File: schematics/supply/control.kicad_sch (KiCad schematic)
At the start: 102 parts, among them J10 Conn_01x04_Pin, J11 Conn_01x04_Pin, J12 Conn_01x04_Pin, J13 Conn_01x04_Pin, J14 USBASP, J15 USBASP, J16 JST XH B3B, J17 Conn_01x06_Pin, J18 Conn_01x03_Pin, J19 Conn_01x06_Pin, M1 Fan, Q10 IRLML5203, Q3 IRLML0030, Q4 IRLML0030, Q6 IRLML0030, SW1 EC11W****, SW3 SW_Push, U14 ATmega328-A, U15 ATtiny1616-M, U16 Display_1.18inch_st7535, U17 AD9833xRM, U18 MCP4726A0T-E/CH, U19 MAX961, U20 LM158DR, U21 FAN3100, X1 HC-49U, 16MHz, X2 25 MHz

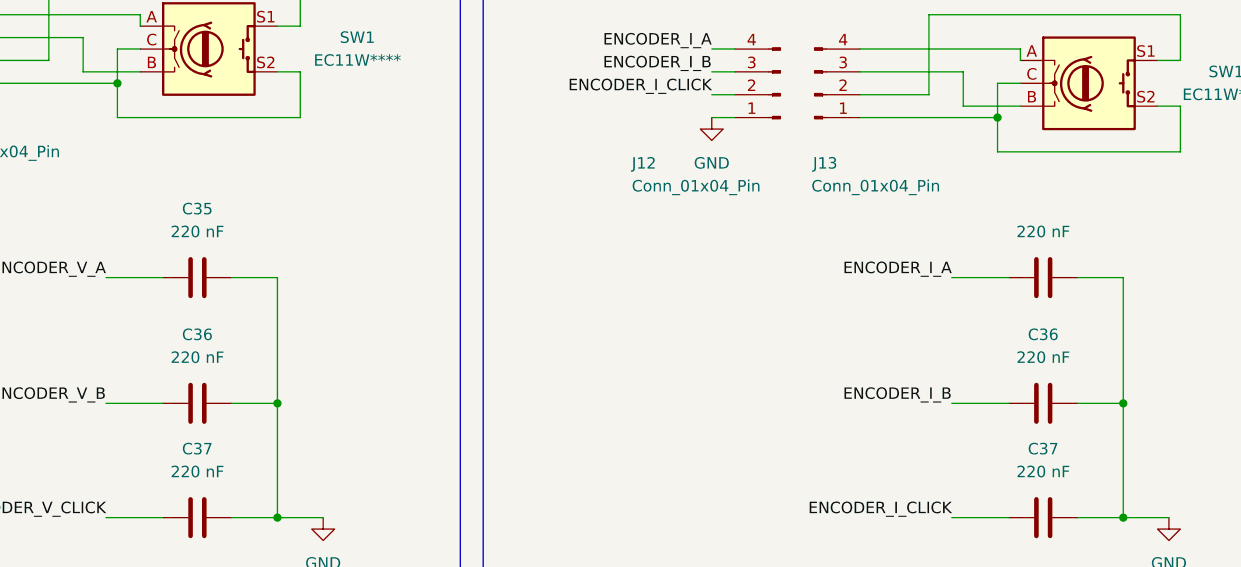
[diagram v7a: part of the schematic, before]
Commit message: some changes in schema. I found additional error. This commit saves changes before re-write some blocks
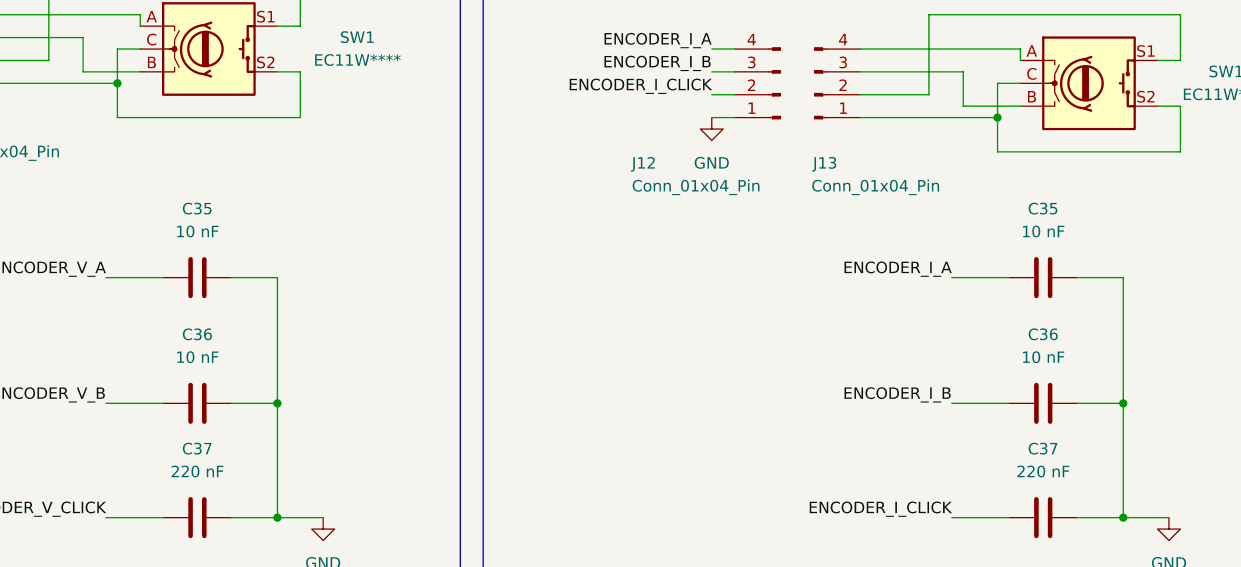
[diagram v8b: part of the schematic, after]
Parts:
- C35, C36: value 220 nF -> 10 nF
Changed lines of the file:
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@@
 			)
 		)
-		(property "Value" "220 nF"
+		(property "Value" "10 nF"
 			(at 77.47 165.1 90)
 			(effects
@@
 					(size 1.27 1.27)
 				)
-				(hide yes)
 			)
 		)
-		(property "Value" "220 nF"
+		(property "Value" "10 nF"
 			(at 171.45 165.1 90)
 			(effects
@@
 			)
 		)
-		(property "Value" "220 nF"
+		(property "Value" "10 nF"
 			(at 77.47 179.07 90)
 			(effects
@@
 			)
 		)
-		(property "Value" "220 nF"
+		(property "Value" "10 nF"
 			(at 171.45 179.07 90)
 			(effects
